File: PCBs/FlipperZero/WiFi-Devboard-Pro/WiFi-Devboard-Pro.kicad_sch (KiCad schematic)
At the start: 26 parts

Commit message: add libs, update schematics
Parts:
- removed J?: Micro_SD_Card_Det, Connector_Card:microSD_HC_Hirose_DM3D-SF, symbol Connector:Micro_SD_Card_Det
- added J?: (no value), symbol 5033981892:5033981892
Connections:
- net +3V3: now also J?.4 (VDD)
- net GND: now also J?.6 (VSS)
- net SD-CLK: now also J?.5 (CLK)
- net SD-CMD: now also J?.3 (CMD)
- net SD-Data0: now also J?.7 (DAT0)
- net SD-Data1: now also J?.8 (DAT1)
- net SD-Data2: now also J?.1 (DAT2)
- net SD-Data3: now also J?.2 (CD/DAT3)
- net SD-Det: now also J?.10 (DETECT_SWITCH), J?.9 (DETECT_LEVEL)
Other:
- moved on the sheet: J?

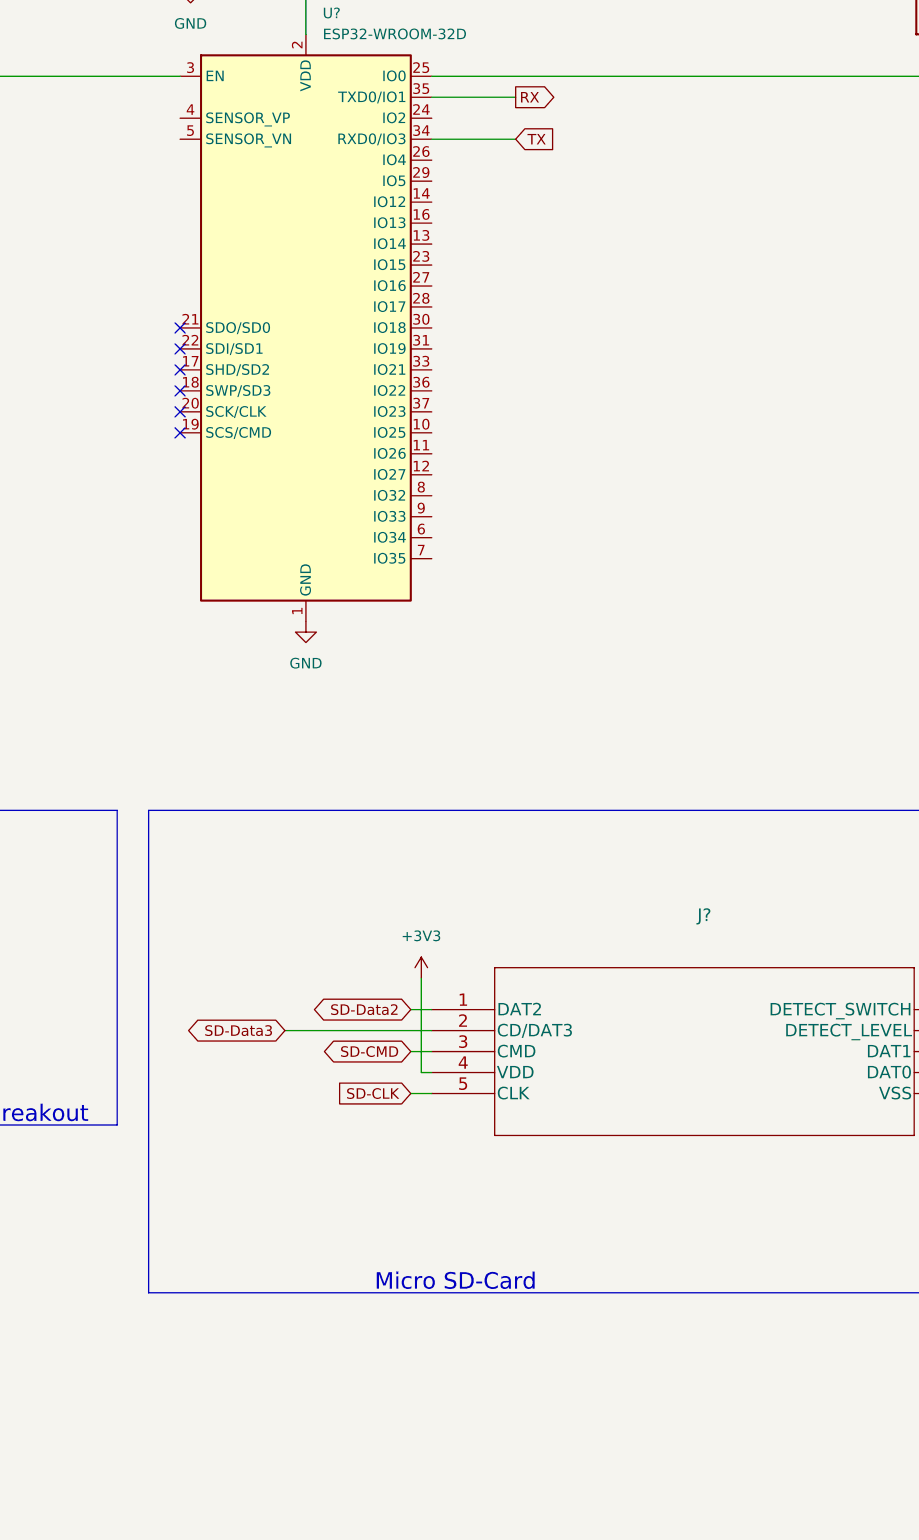
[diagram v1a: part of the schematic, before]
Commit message: Add RGB LED
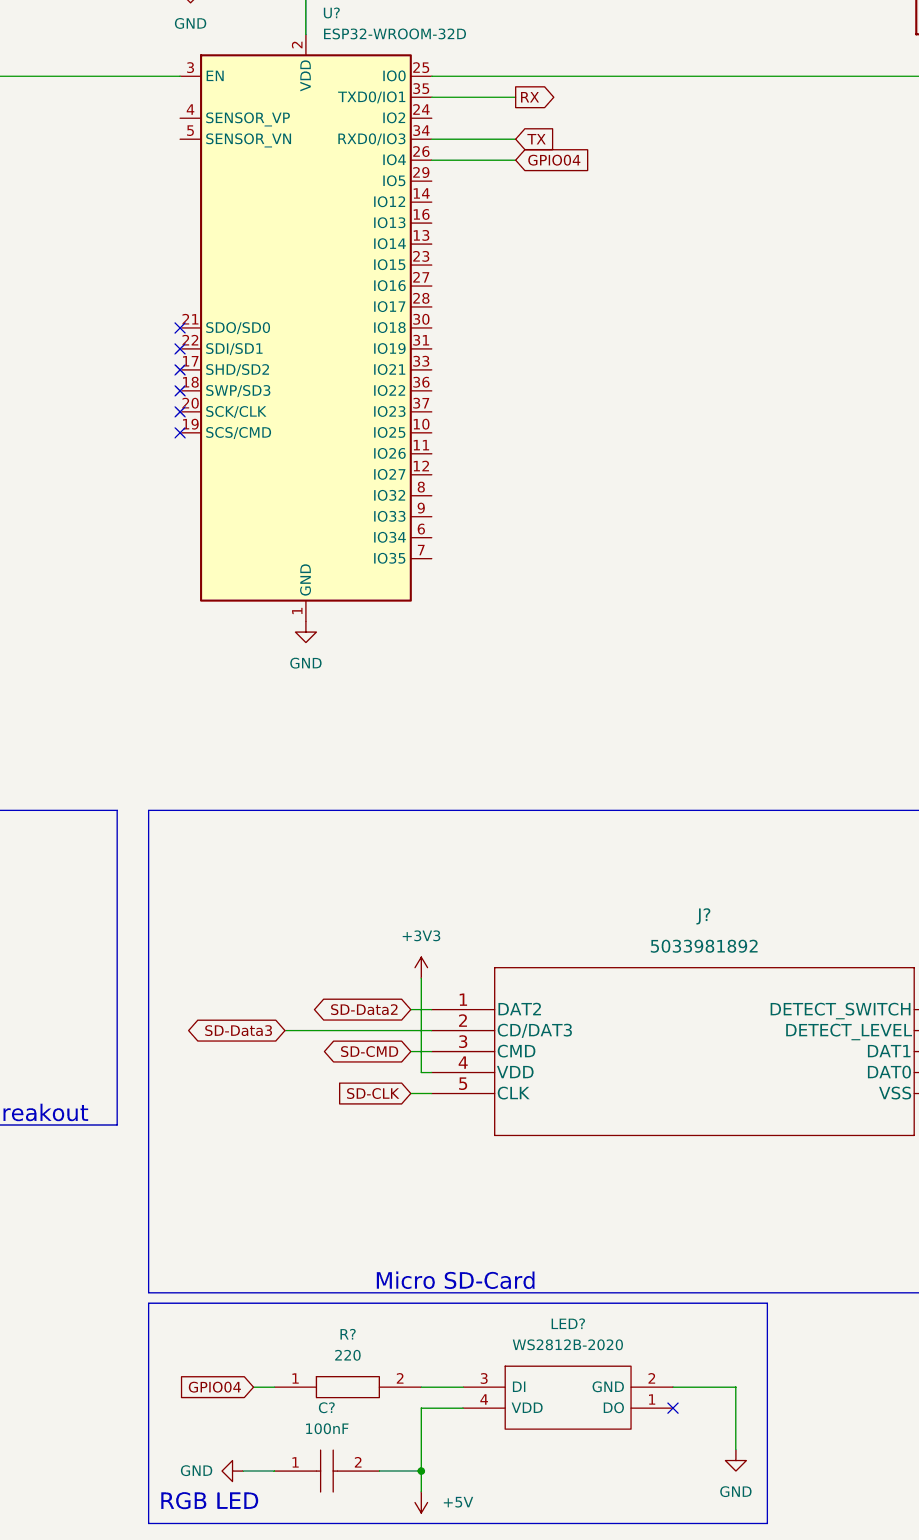
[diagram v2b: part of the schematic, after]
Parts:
- added C?: 100nF, CAPC1005X55N, symbol SamacSys_Parts:CC0402KRX7R7BB104
- added LED?: WS2812B-2020, WS2812B2020, symbol SamacSys_Parts:WS2812B-2020
- added R?: 220, RESC1005X40N, symbol SamacSys_Parts:RC0402FR-07220RL
- J?: value (none) -> 5033981892; footprint (none) -> Libraries:5033981892
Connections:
- net +5V: now also C?.2, LED?.4 (VDD)
- net GND: now also C?.1, LED?.2 (GND)
- net GPIO04: now reaches U?.26 (IO4)
- net GPIO04: now also R?.1
- new net: LED?.3 (DI), R?.2
- no-connect marks 6 -> 7
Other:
- note added: "RGB LED"

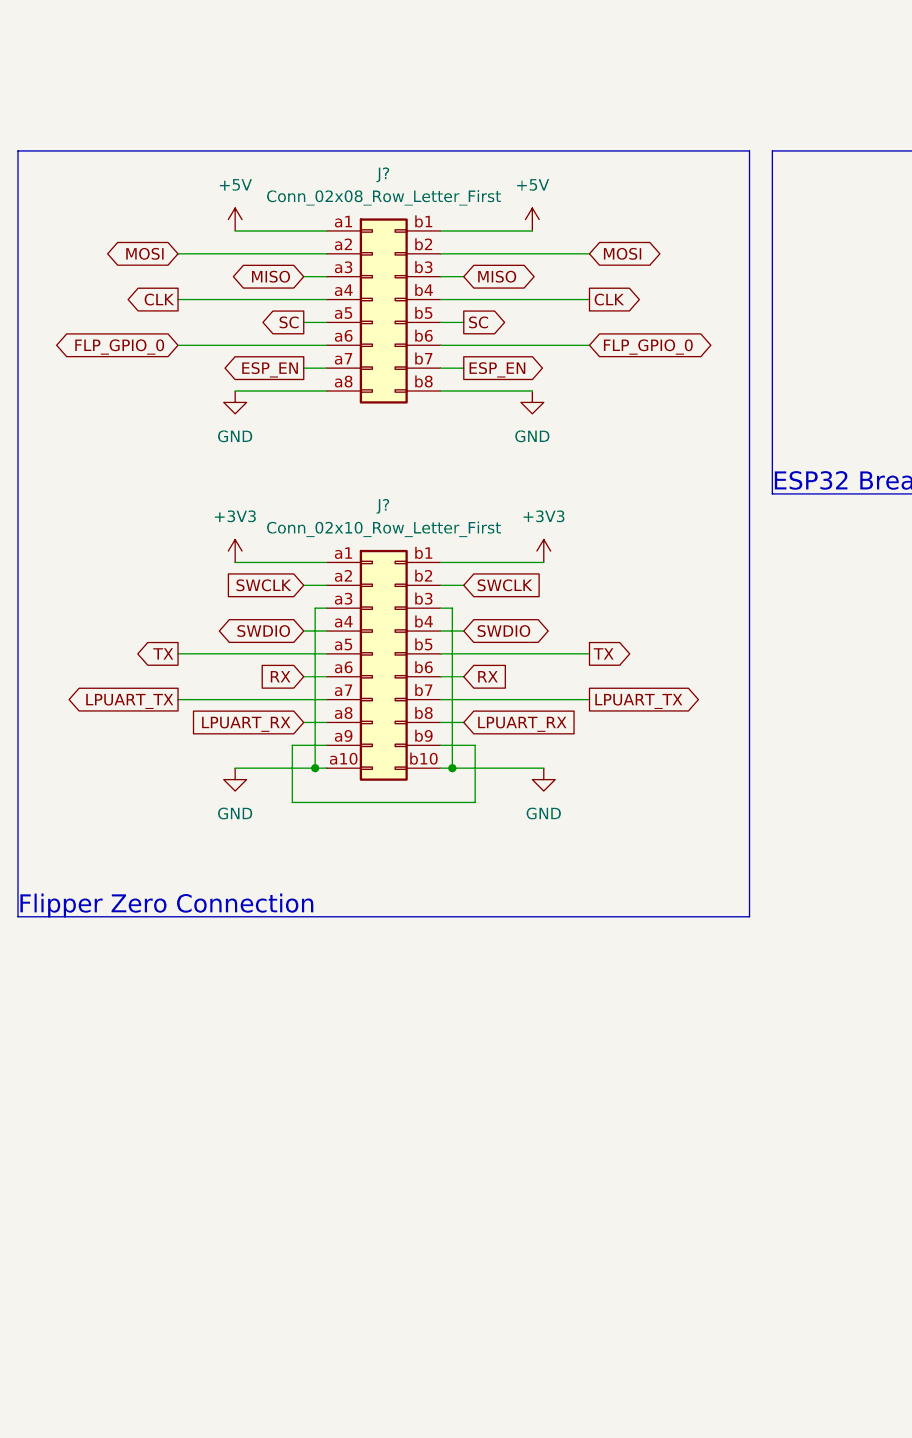
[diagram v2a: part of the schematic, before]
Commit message: Update flipper header and JTAG
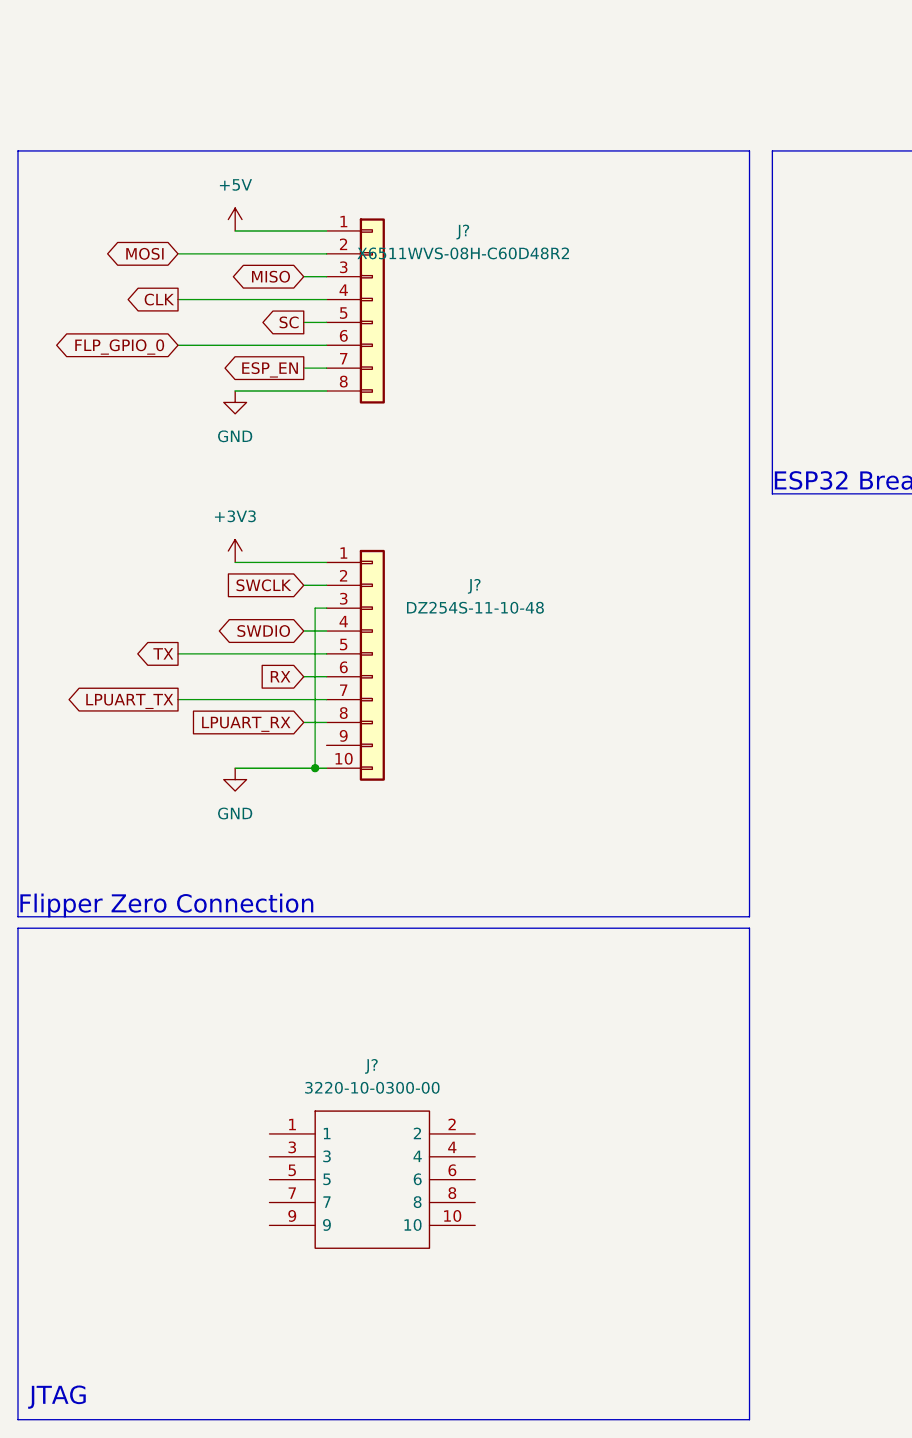
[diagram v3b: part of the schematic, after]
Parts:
- removed J?: Conn_02x10_Row_Letter_First, symbol Connector_Generic:Conn_02x10_Row_Letter_First
- removed J?: Conn_02x08_Row_Letter_First, symbol Connector_Generic:Conn_02x08_Row_Letter_First
- added J?: X6511WVS-08H-C60D48R2, HUSRSP8W66P254_2000X250X850P, symbol Connector_Generic:Conn_01x08
- added J?: 3220-10-0300-00, 322010030000, symbol SamacSys_Parts:3220-10-0300-00
- added J?: DZ254S-11-10-48, HUSRSP10W66P254_2500X250X850P, symbol Connector_Generic:Conn_01x10
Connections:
- net +3V3: now also J?.1 (Pin_1)
- net +5V: now also J?.1 (Pin_1)
- net CLK: now also J?.4 (Pin_4)
- net ESP_EN: now also J?.7 (Pin_7)
- net FLP_GPIO_0: now also J?.6 (Pin_6)
- net GND: now also J?.10 (Pin_10), J?.3 (Pin_3), J?.8 (Pin_8)
- net LPUART_RX: now also J?.8 (Pin_8)
- net LPUART_TX: now also J?.7 (Pin_7)
- net MISO: now also J?.3 (Pin_3)
- net MOSI: now also J?.2 (Pin_2)
- net RX: now also J?.6 (Pin_6)
- net SC: now also J?.5 (Pin_5)
- net SWCLK: now also J?.2 (Pin_2)
- net SWDIO: now also J?.4 (Pin_4)
- net TX: now also J?.5 (Pin_5)
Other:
- note added: "JTAG"

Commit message: Update footprint for ESP32 and micro SD
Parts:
- removed J?: 5033981892, Libraries:5033981892, symbol 5033981892:5033981892
- removed U?: ESP32-WROOM-32D, RF_Module:ESP32-WROOM-32, symbol RF_Module:ESP32-WROOM-32D
- added IC?: ESP32-WROOM-32E-N4, ESP32WROOM32EN4, symbol SamacSys_Parts:ESP32-WROOM-32E-N4
- added J?: 503398-1892, 503398-1892, symbol SamacSys_Parts:503398-1892
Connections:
- net +3V3: now also IC?.2 (3V3), J?.4 (VDD)
- net GND: now also IC?.1 (GND_1), J?.6 (VSS)
- net GPIO04: now also IC?.26 (IO4)
- net RX: now also IC?.35 (TXD0)
- net SD-CLK: now also J?.5 (CLK)
- net SD-CMD: now also J?.3 (CMD)
- net SD-Data0: now also J?.7 (DAT0)
- net SD-Data1: now also J?.8 (DAT1)
- net SD-Data2: now also J?.1 (DAT2)
- net SD-Data3: now also J?.2 (CD/DAT3)
- net SD-Det: now also J?.10 (DETECT_SWITCH), J?.9 (DETECT_LEVER)
- net TX: now also IC?.34 (RXD0)
- net at R?.2, SW?.1: now also IC?.25 (IO0)
- net at C?.1, R?.2, SW?.2: now also IC?.3 (EN)
- no-connect marks 7 -> 1
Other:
- moved on the sheet: IC?, R?, U?

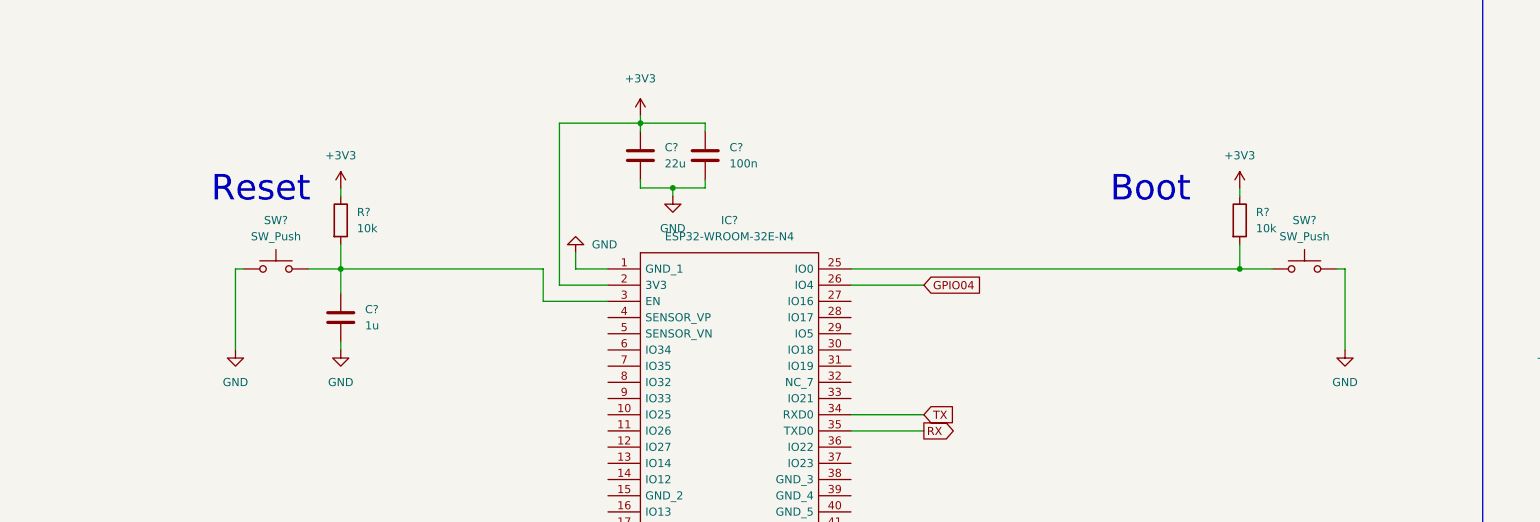
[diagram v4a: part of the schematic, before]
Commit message: Add Marauder logo and update components
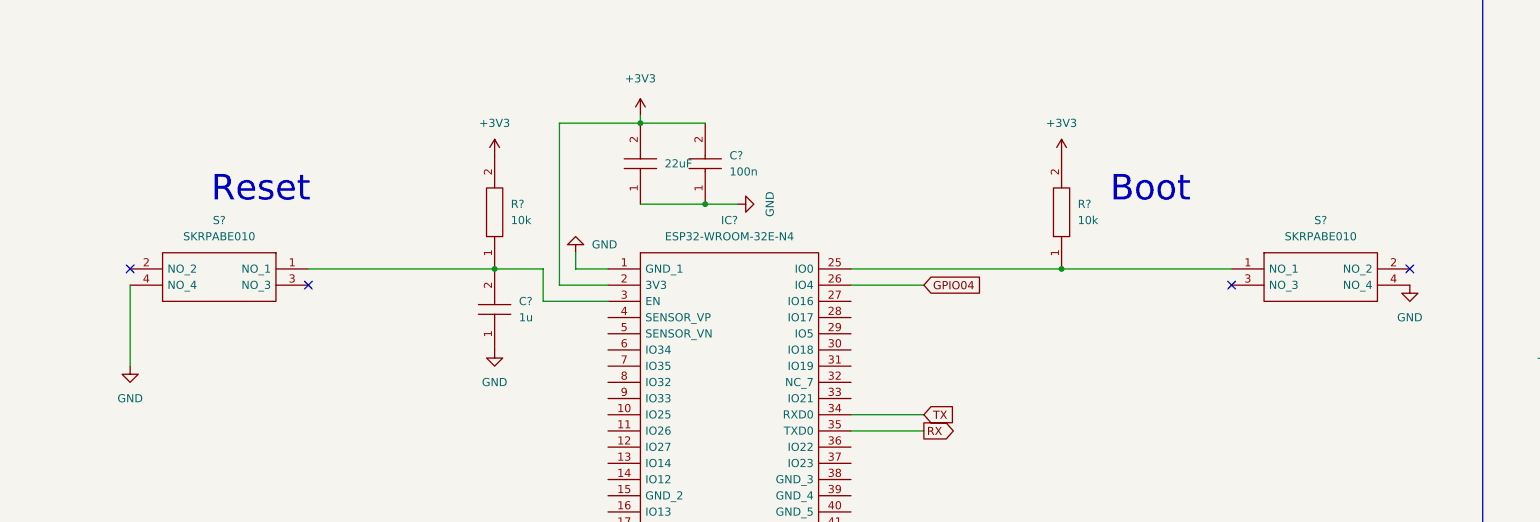
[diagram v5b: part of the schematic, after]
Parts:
- removed C?: 22u, symbol Device:C
- removed C?: 100n, symbol Device:C
- removed C?: 1u, symbol Device:C
- removed R? (x2): 10k, symbol Device:R
- removed SW? (x2): SW_Push, symbol Switch:SW_Push
- added C?: 1u, CAPC1005X60N, symbol SamacSys_Parts:CL05A105KA5NQNC
- added C?: 100n, CAPC1005X55N, symbol SamacSys_Parts:CL05B104KO5NNNC
- added C?: 22uF, CAPC1005X80N, symbol SamacSys_Parts:CM05X5R226M06AH080
- added R? (x2): 10k, RESC1005X40N, symbol SamacSys_Parts:RC0402FR-0710KL
- added S? (x2): SKRPABE010, SKRPABE010, symbol SamacSys_Parts:SKRPABE010
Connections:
- net +3V3: now also C?.2, C?.2, R?.2, R?.2
- net GND: now also C?.1, C?.1, C?.1, S?.4 (NO_4), S?.4 (NO_4)
- net at IC?.25 (IO0): now also R?.1, S?.1 (NO_1)
- net at IC?.3 (EN): now also C?.2, R?.1, S?.1 (NO_1)
- no-connect marks 1 -> 5
